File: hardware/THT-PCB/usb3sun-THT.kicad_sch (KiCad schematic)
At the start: 52 parts, among them J1 Conn_01x04, J2 8918-P8B, J3 USB-U267-BWS, Q1 2N7002DW, Q2 2N7002DW, Q3 2N7002DW, Q4 MMBT2222A, Q5 MMBT2222A, SW1 TS-1187A-B-A-B, U1 Pico, U2 SRV05-4, U3 SRV05-4, U4 MAX40200AUK, U5 MAX40200AUK

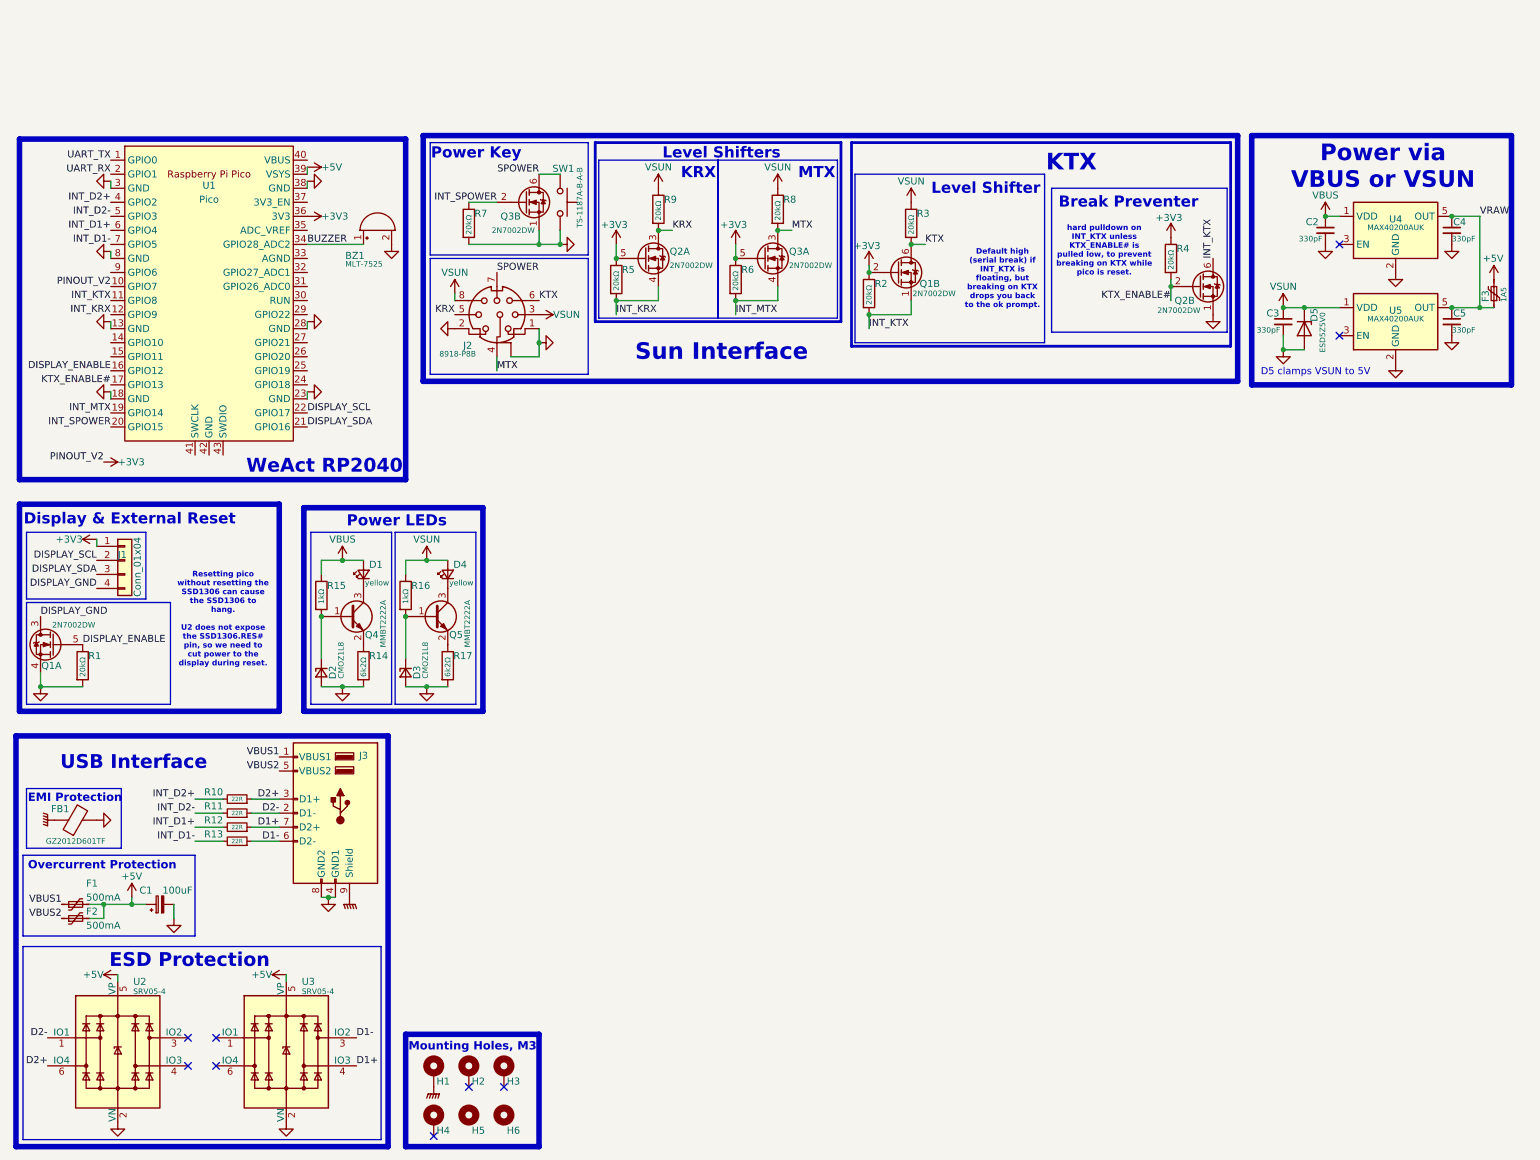
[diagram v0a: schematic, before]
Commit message: Change fets to match original refs
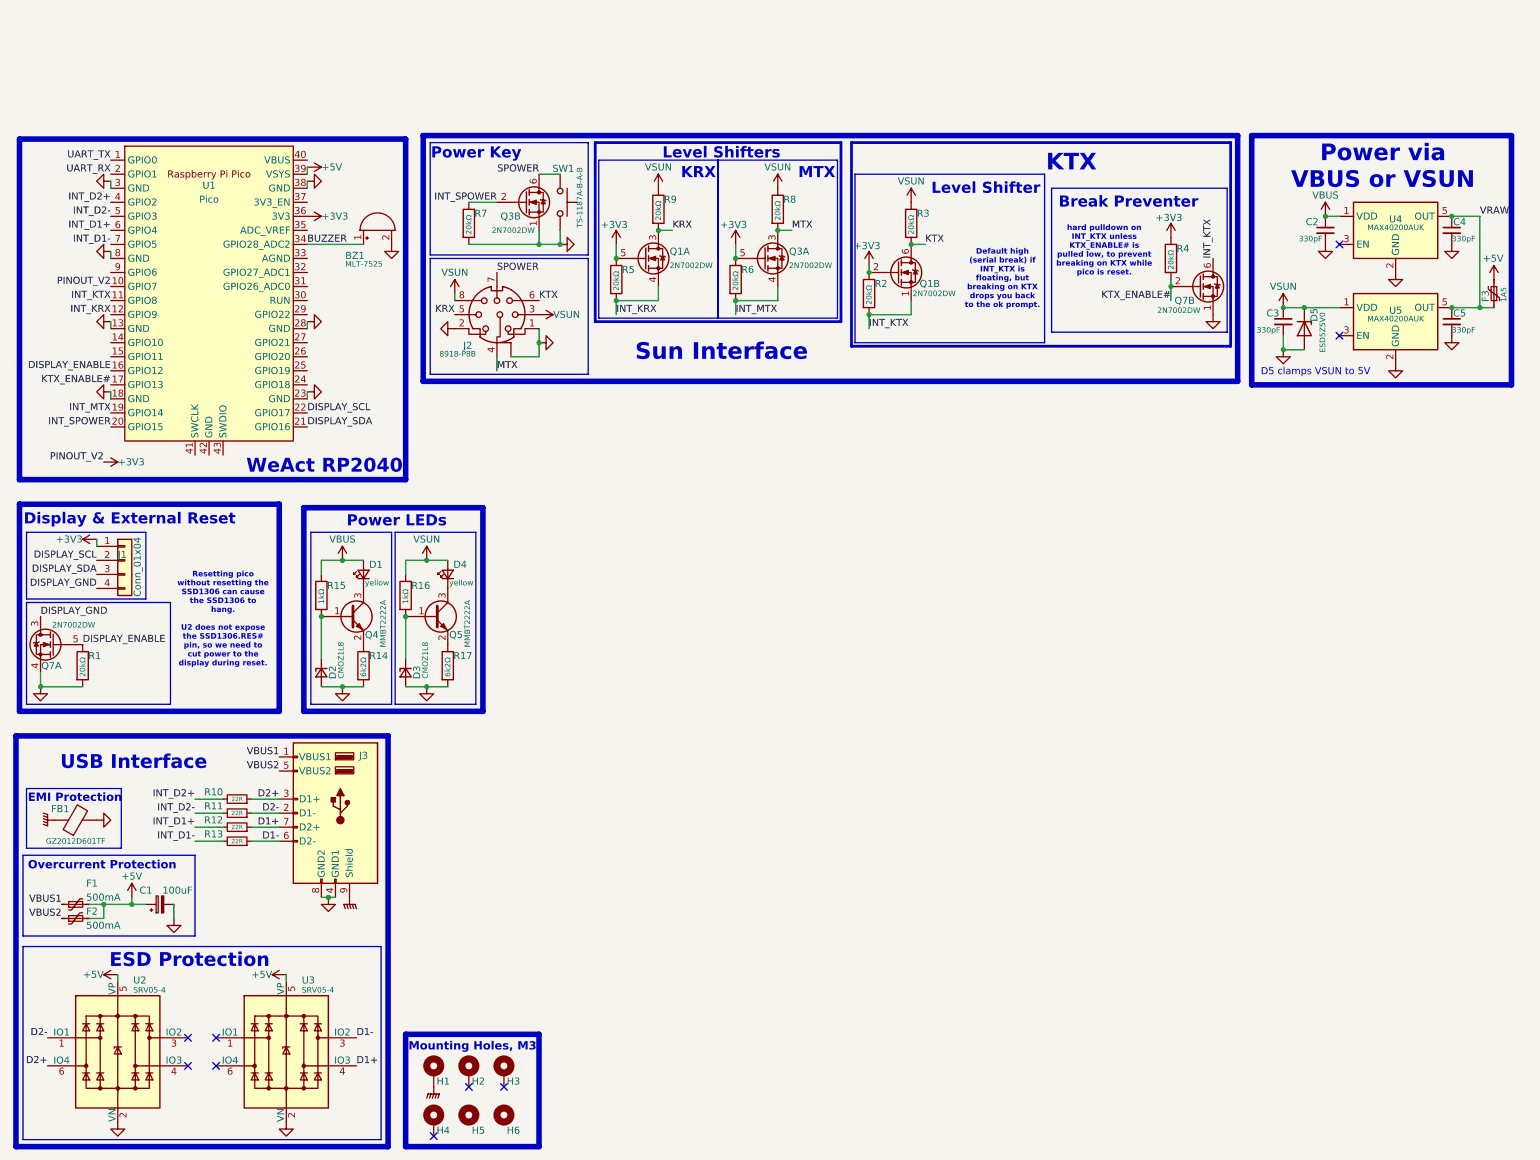
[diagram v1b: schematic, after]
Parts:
- renumbered Q2 to Q1, Q2 to Q7, Q1 to Q7
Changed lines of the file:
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@@
 		(on_board yes)
 		(dnp no)
-		(property "Reference" "Q2"
+		(property "Reference" "Q7"
 			(at 226.568 43.18 0)
 			(effects
@@
 			(project "usb3sun-THT"
 				(path "/e8fc4e41-10af-441f-8282-dd879bdc5d08"
-					(reference "Q2")
+					(reference "Q7")
 					(unit 2)
 				)
@@
 		(dnp no)
 		(property "Reference" "U3"
-			(at 65.024 166.37 0)
+			(at 65.024 166.116 0)
 			(effects
 				(font
@@
 		)
 		(property "Value" "SRV05-4"
-			(at 65.024 168.148 0)
+			(at 65.024 167.894 0)
 			(effects
 				(font
@@
 		(on_board yes)
 		(dnp no)
-		(property "Reference" "Q1"
+		(property "Reference" "Q7"
 			(at 21.59 109.22 0)
 			(effects
@@
 			(project "usb3sun-THT"
 				(path "/e8fc4e41-10af-441f-8282-dd879bdc5d08"
-					(reference "Q1")
+					(reference "Q7")
 					(unit 1)
 				)
@@
 		(on_board yes)
 		(dnp no)
-		(property "Reference" "Q2"
+		(property "Reference" "Q1"
 			(at 131.572 34.29 0)
 			(effects
@@
 			(project "usb3sun-THT"
 				(path "/e8fc4e41-10af-441f-8282-dd879bdc5d08"
-					(reference "Q2")
+					(reference "Q1")
 					(unit 1)
 				)
@@
 		(dnp no)
 		(property "Reference" "U2"
-			(at 34.544 166.37 0)
+			(at 34.544 166.116 0)
 			(effects
 				(font
@@
 		)
 		(property "Value" "SRV05-4"
-			(at 34.544 168.148 0)
-			(effects
-				(font
+			(at 34.544 167.894 0)
+			(effects
+				(font

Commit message: SCH Complete; Begin PCB work!
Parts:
- removed J1: Conn_01x04, symbol Connector_Generic:Conn_01x04
- added U6: ~, KiCad-SSD1306-0.91-OLED-4pin-128x32:SSD1306-0.91-OLED-4pin-128x32, symbol usb3sun:SSD1306_4pin
- BZ1: value MLT-7525 -> SEA-1285F; footprint Buzzer_Beeper:PUIAudio_SMT_0825_S_4_R -> Buzzer_Beeper:Buzzer_12x9.5RM7.6; LCSC C95299 -> C2693577
- R1, R14, R15, R16, R17, R2, R3, R4, R5, R6, R7, R8, R9: footprint (none) -> Resistor_THT:R_Axial_DIN0207_L6.3mm_D2.5mm_P10.16mm_Horizontal
- R10, R11, R12, R13: footprint Resistor_SMD:R_0402_1005Metric -> Resistor_THT:R_Axial_DIN0207_L6.3mm_D2.5mm_P10.16mm_Horizontal
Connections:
- net +3V3: now also U6.2 (VCC)
- net DISPLAY_GND: now also U6.1 (GND)
- net DISPLAY_SCL: now also U6.3 (SCL)
- net DISPLAY_SDA: now also U6.4 (SDA)
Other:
- note added: "2N7002DW REALLY SMOL FIND BIGGER"
- note added: "MMBT2222A SMOL BUT HAND-SOLDERABLE I THINK"
- moved on the sheet: Q7A, R1

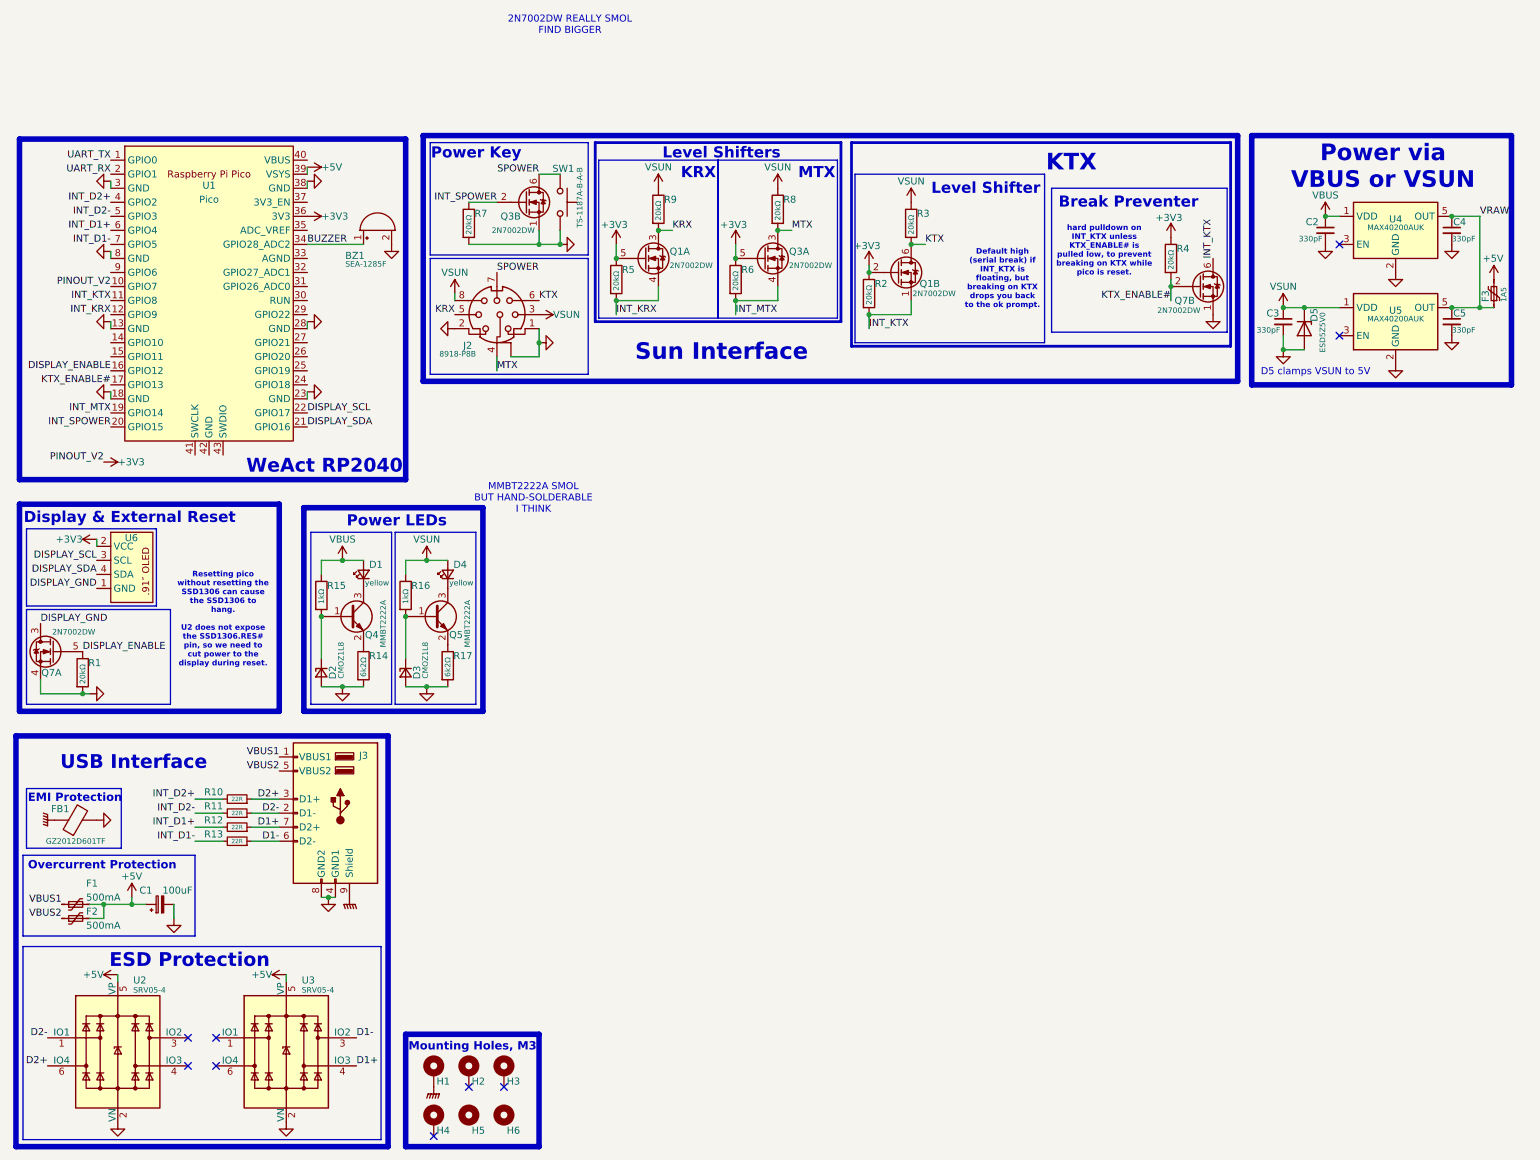
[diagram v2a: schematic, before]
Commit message: Simplification of LED circuits
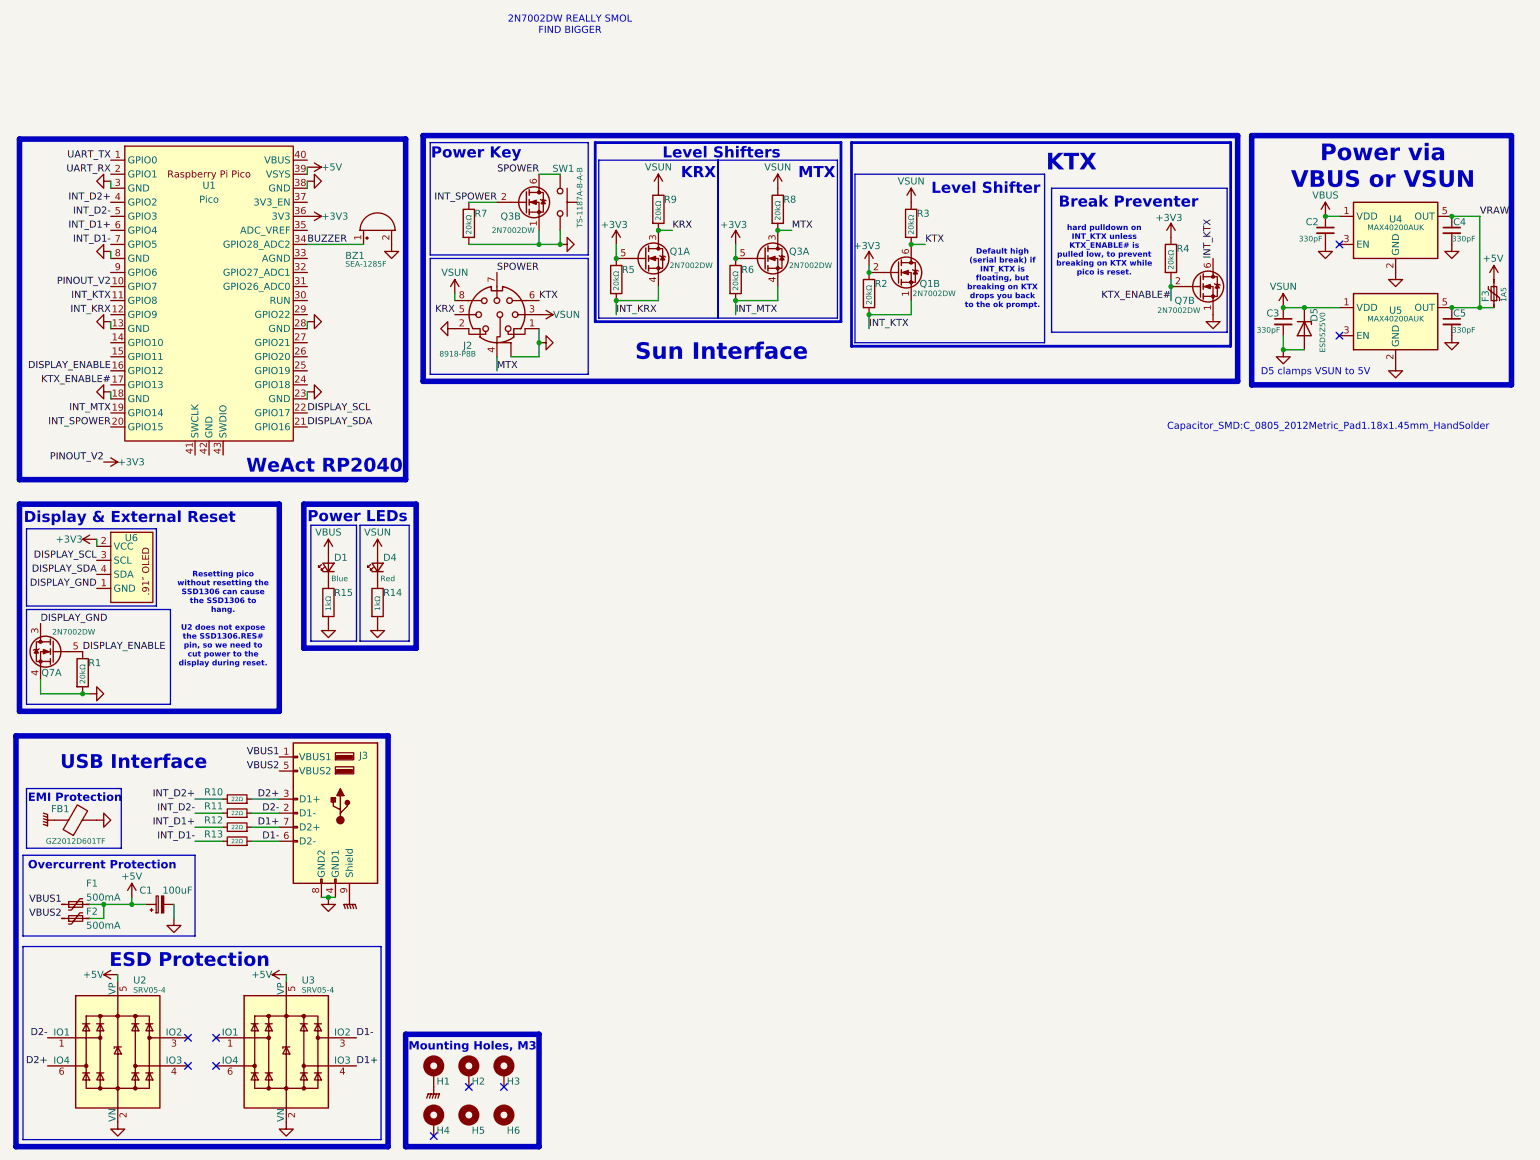
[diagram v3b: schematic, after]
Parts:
- removed D2, D3: CMOZ1L8, Diode_SMD:D_SOD-523, symbol Device:D_Zener_Small
- removed Q4, Q5: MMBT2222A, Package_TO_SOT_SMD:SOT-23, symbol Transistor_BJT:MMBT5550L
- removed R16: 1kΩ, Resistor_THT:R_Axial_DIN0207_L6.3mm_D2.5mm_P10.16mm_Horizontal, symbol Device:R
- removed R17: 6k2Ω, Resistor_THT:R_Axial_DIN0207_L6.3mm_D2.5mm_P10.16mm_Horizontal, symbol Device:R
- C2, C3, C4, C5: footprint Capacitor_SMD:C_0603_1608Metric -> Capacitor_SMD:C_0805_2012Metric_Pad1.18x1.45mm_HandSolder; LCSC C1664 -> C376975
- D1: value 19-213/Y2C-CQ2R2L/3T(CY) -> (none); footprint LED_SMD:LED_0603_1608Metric -> LED_THT:LED_D3.0mm; LCSC C72038 -> C2895474; colour yellow -> Blue
- D4: value 19-213/Y2C-CQ2R2L/3T(CY) -> (none); footprint LED_SMD:LED_0603_1608Metric -> LED_THT:LED_D3.0mm; LCSC C72038 -> C440523; colour yellow -> Red
- R10, R11, R12, R13: value 22R -> 22Ω
- R14: value 6k2Ω -> 1kΩ
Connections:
- net GND: now also R15.2
- net VBUS: no longer R15.1
- net at D4.1 (K): now also R14.1
- net at D1.1 (K): now also R15.1
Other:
- note added: "Capacitor_SMD:C_0805_2012Metric_Pad1.18x1.45mm_HandSolder"
- note removed: "MMBT2222A SMOL BUT HAND-SOLDERABLE I THINK"
- moved on the sheet: D1, D4

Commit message: SCH Improvements
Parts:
- removed H5, H6: MountingHole, MountingHole:MountingHole_3.2mm_M3_DIN965, symbol Mechanical:MountingHole
- D1, D4: value (none) -> ~
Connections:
- net GNDPWR: no longer H1.1
- no-connect marks 9 -> 28
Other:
- moved on the sheet: H3, H4
